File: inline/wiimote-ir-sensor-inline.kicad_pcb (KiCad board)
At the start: 2 copper layers, 13 x 16.6 mm, 10 parts, among them J1 Conn_01x04_Pin, U2 AP2112-3.3V, X1 SG3225CAN 24.0000M-TJGA3

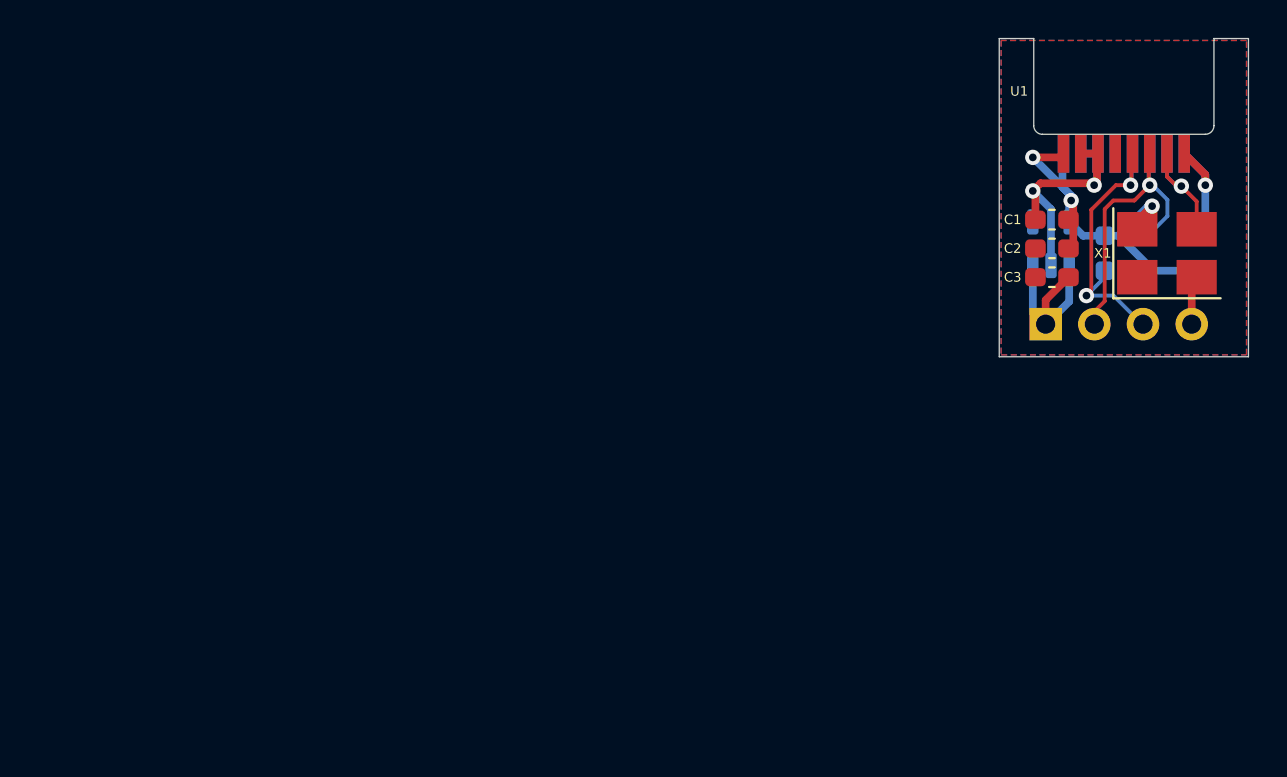
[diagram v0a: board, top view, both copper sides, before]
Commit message: Revision 2.
- Reroute to leave more empty space on sides
- Tweak camera footprint
- Add castellated variant
- Add manually panelised boards to help prevent panel tabs
  from appearing in edge connector
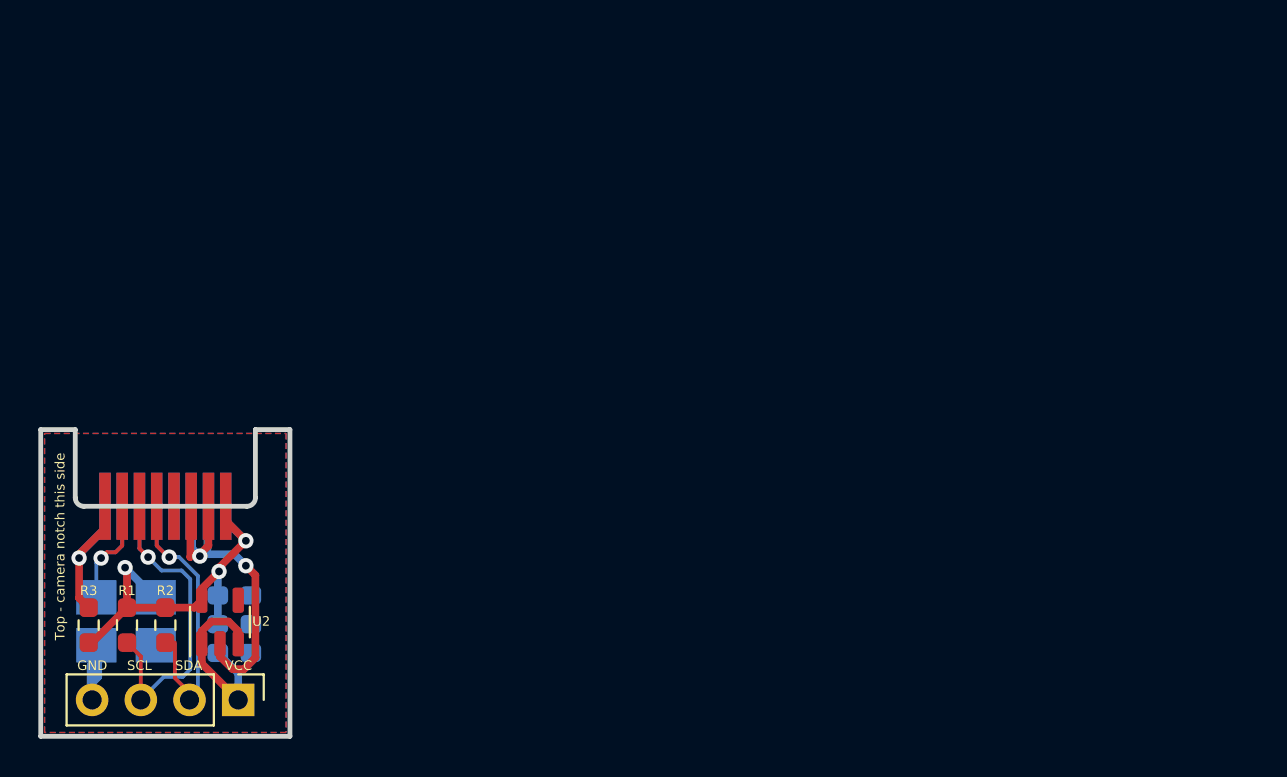
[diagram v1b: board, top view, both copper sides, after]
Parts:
- C1, C2, C3, U1, X1: moved to B.Cu
- J1, R1, R2, R3, U2: moved to F.Cu
- moved R3 60.7 mm to (102.5, 110.2)
- moved X1 57.6 mm to (104.5, 110.0), turned to 180 degrees
- moved R1 56.7 mm to (104.5, 110.2), turned to -90 degrees
- moved U1 53.6 mm to (106.5, 101.5), turned to 180 degrees
- moved R2 52.7 mm to (106.5, 110.2)
- moved U2 47.6 mm to (109.3, 110.0)
- moved C1 46.9 mm to (110.1, 108.7), turned to 0 degrees
- moved C2 46.9 mm to (110.1, 110.2), turned to 0 degrees
- moved C3 46.9 mm to (110.1, 111.7), turned to 0 degrees
- moved J1 46.5 mm to (110.3, 114.1)
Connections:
- J1 pad 2: /SDA -> /SCL
- J1 pad 3: /SCL -> /SDA
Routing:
- net GND: track 17.2 -> 24.9 mm
- net /SDA: track 16.2 -> 19.6 mm
- net /SCL: track 15.8 -> 18.4 mm, vias 2 -> 1
- net /CLK: track 6.90 -> 8.79 mm
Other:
- board size 13 x 16.6 mm -> 13 x 16 mm
